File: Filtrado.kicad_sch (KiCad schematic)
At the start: 31 parts

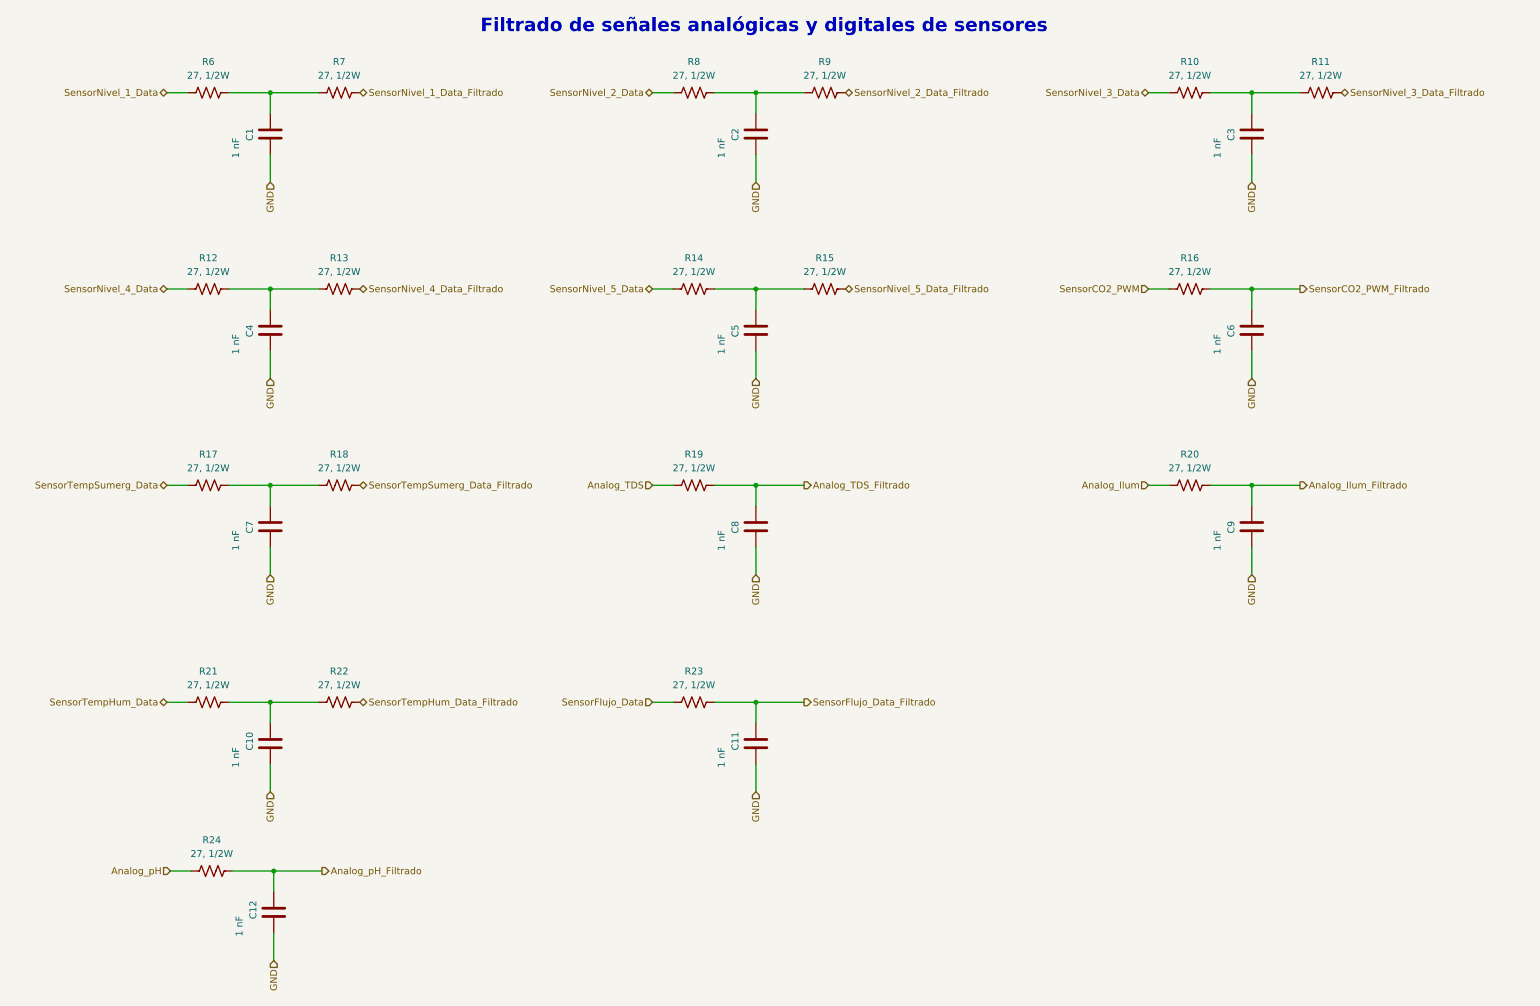
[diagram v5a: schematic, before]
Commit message: Se finalizó con el PCB del prototipo.
Dado que se buscó a toda costa que el PCB fuera de 1 capa, en varios puntos del circuito se tuvieron que agregar pin headers individuales para conectar a 3V3 y GND, junto con tiras de pin headers. Cada una de estas se conectara luego entre si mediante cables.

Tambien se generaron los archivos Gerber y BOM.
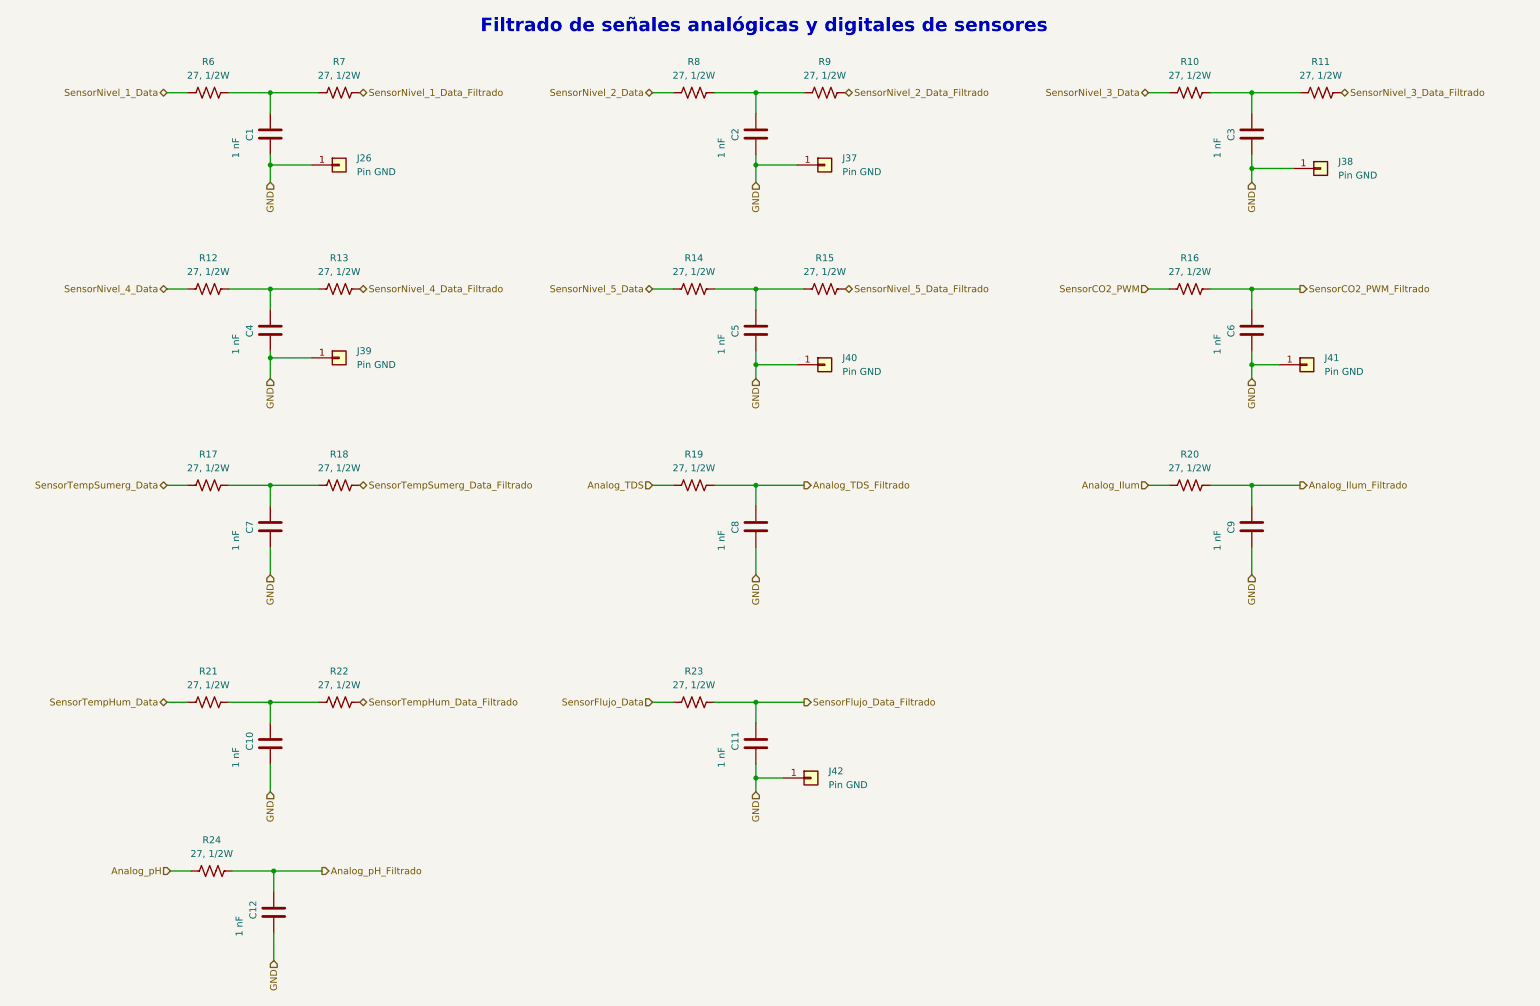
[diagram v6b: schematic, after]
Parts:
- added J26, J37, J38, J39, J40, J41, J42: Pin GND, Connector_PinHeader_2.54mm:PinHeader_1x01_P2.54mm_Vertical, symbol Connector_Generic:Conn_01x01
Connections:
- net GND: now also J26.1 (Pin_1), J37.1 (Pin_1), J38.1 (Pin_1), J39.1 (Pin_1), J40.1 (Pin_1), J41.1 (Pin_1), J42.1 (Pin_1)

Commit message: Se modificaron algunos componentes, según disponibilidad
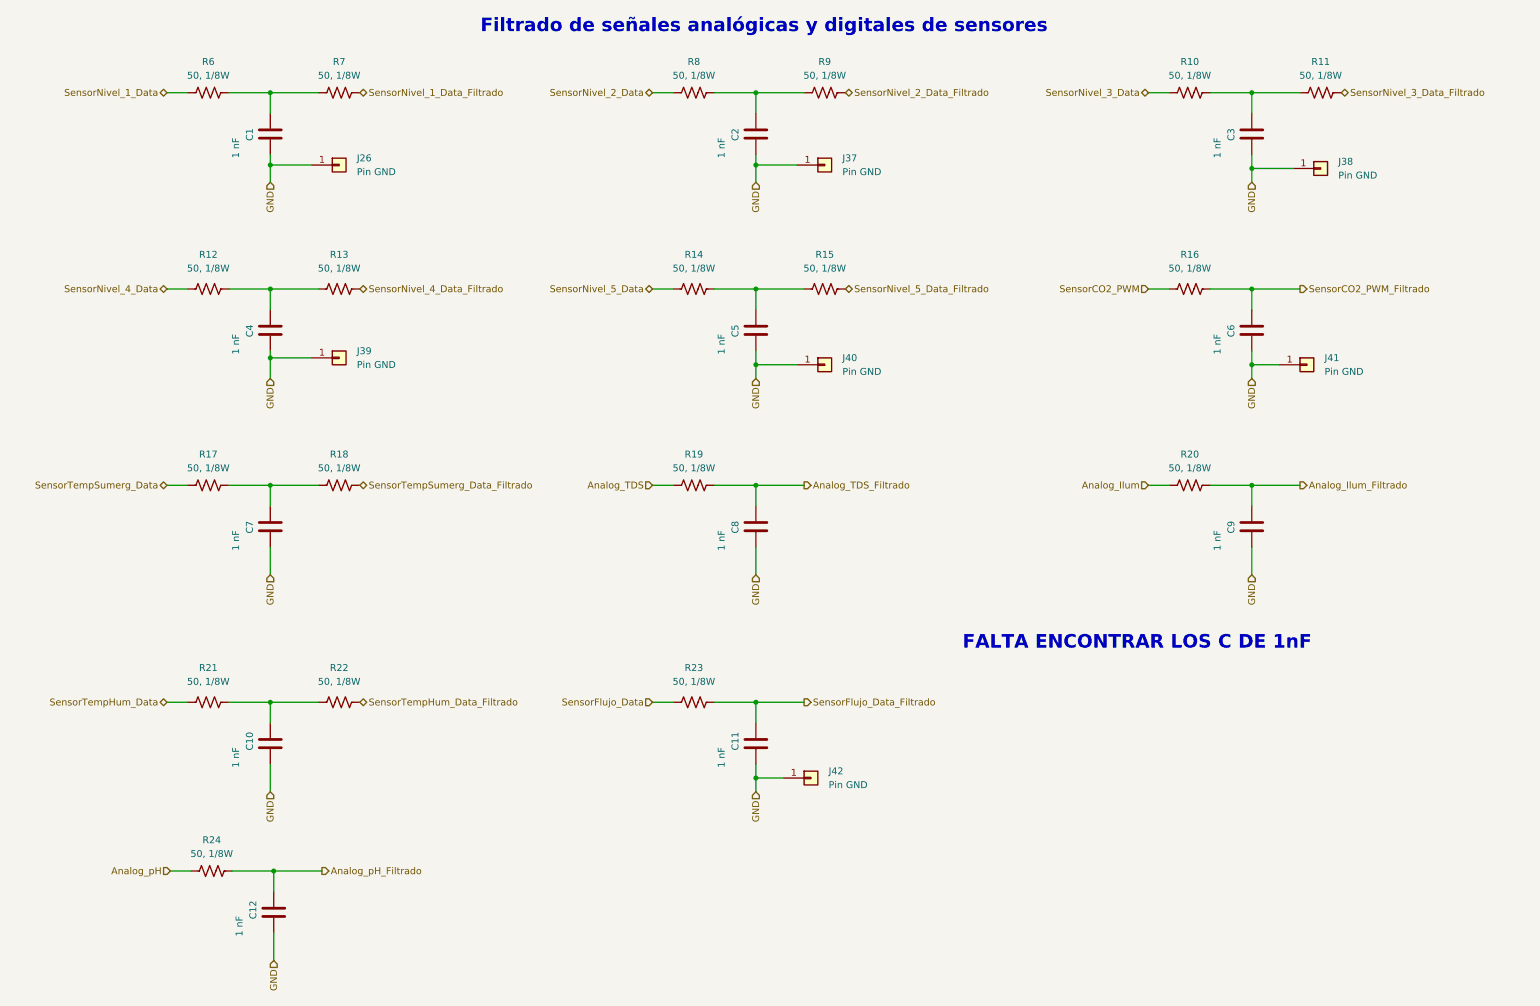
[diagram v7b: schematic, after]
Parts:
- R10, R11, R12, R13, R14, R15, R16, R17, R18, R19, R20, R21, R22, R23, R24, R6, R7, R8, R9: value 27, 1/2W -> 50, 1/8W
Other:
- note added: "FALTA ENCONTRAR LOS C DE 1nF"
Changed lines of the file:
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@@
     (stroke (width 0) (type default) (color 0 0 0 0))
+  )
+  (text "FALTA ENCONTRAR LOS C DE 1nF" (at 185.42 131.445 0)
+    (effects (font (size 2.5 2.5) (thickness 0.4) bold) (justify left bottom))
   )
   (text "Filtrado de señales analógicas y digitales de sensores"
@@
   (symbol (lib_id "Device:R_US") (at 160.02 64.77 90) (unit 1)
     (in_bom yes) (on_board yes) (fields_autoplaced)
-    (property "Reference" "R15" (id 0) (at 160.02 59.055 90))
-    (property "Value" "27, 1/2W" (id 1) (at 160.02 61.595 90))
+    (property "Reference" "R15" (id 0) (at 160.02 58.42 90))
+    (property "Value" "50, 1/8W" (id 1) (at 160.02 60.96 90))
     (property "Footprint" "Resistor_SMD:R_0805_2012Metric" (id 2) (at 160.274 63.754 90)
       (effects (font (size 1.27 1.27)) hide)
@@
     (in_bom yes) (on_board yes) (fields_autoplaced)
     (property "Reference" "R7" (id 0) (at 70.485 22.86 90))
-    (property "Value" "27, 1/2W" (id 1) (at 70.485 25.4 90))
+    (property "Value" "50, 1/8W" (id 1) (at 70.485 25.4 90))
     (property "Footprint" "Resistor_SMD:R_0805_2012Metric" (id 2) (at 70.739 27.559 90)
       (effects (font (size 1.27 1.27)) hide)
@@
   (symbol (lib_id "Device:R_US") (at 227.33 64.77 90) (unit 1)
     (in_bom yes) (on_board yes) (fields_autoplaced)
-    (property "Reference" "R16" (id 0) (at 227.33 59.055 90))
-    (property "Value" "27, 1/2W" (id 1) (at 227.33 61.595 90))
+    (property "Reference" "R16" (id 0) (at 227.33 58.42 90))
+    (property "Value" "50, 1/8W" (id 1) (at 227.33 60.96 90))
     (property "Footprint" "Resistor_SMD:R_0805_2012Metric" (id 2) (at 227.584 63.754 90)
       (effects (font (size 1.27 1.27)) hide)
@@
     (in_bom yes) (on_board yes) (fields_autoplaced)
     (property "Reference" "R24" (id 0) (at 46.99 166.37 90))
-    (property "Value" "27, 1/2W" (id 1) (at 46.99 168.91 90))
+    (property "Value" "50, 1/8W" (id 1) (at 46.99 168.91 90))
     (property "Footprint" "Resistor_SMD:R_0805_2012Metric" (id 2) (at 47.244 171.069 90)
       (effects (font (size 1.27 1.27)) hide)
@@
   (symbol (lib_id "Device:R_US") (at 135.89 64.77 90) (unit 1)
     (in_bom yes) (on_board yes) (fields_autoplaced)
-    (property "Reference" "R14" (id 0) (at 135.89 59.055 90))
-    (property "Value" "27, 1/2W" (id 1) (at 135.89 61.595 90))
+    (property "Reference" "R14" (id 0) (at 135.89 58.42 90))
+    (property "Value" "50, 1/8W" (id 1) (at 135.89 60.96 90))
     (property "Footprint" "Resistor_SMD:R_0805_2012Metric" (id 2) (at 136.144 63.754 90)
       (effects (font (size 1.27 1.27)) hide)
@@
     (in_bom yes) (on_board yes) (fields_autoplaced)
     (property "Reference" "R9" (id 0) (at 160.02 22.86 90))
-    (property "Value" "27, 1/2W" (id 1) (at 160.02 25.4 90))
+    (property "Value" "50, 1/8W" (id 1) (at 160.02 25.4 90))
     (property "Footprint" "Resistor_SMD:R_0805_2012Metric" (id 2) (at 160.274 27.559 90)
       (effects (font (size 1.27 1.27)) hide)
@@
   (symbol (lib_id "Device:R_US") (at 70.485 140.97 90) (unit 1)
     (in_bom yes) (on_board yes) (fields_autoplaced)
-    (property "Reference" "R22" (id 0) (at 70.485 135.255 90))
-    (property "Value" "27, 1/2W" (id 1) (at 70.485 137.795 90))
+    (property "Reference" "R22" (id 0) (at 70.485 134.62 90))
+    (property "Value" "50, 1/8W" (id 1) (at 70.485 137.16 90))
     (property "Footprint" "Resistor_SMD:R_0805_2012Metric" (id 2) (at 70.739 139.954 90)
       (effects (font (size 1.27 1.27)) hide)
@@
     (in_bom yes) (on_board yes) (fields_autoplaced)
     (property "Reference" "R19" (id 0) (at 135.89 95.25 90))
-    (property "Value" "27, 1/2W" (id 1) (at 135.89 97.79 90))
+    (property "Value" "50, 1/8W" (id 1) (at 135.89 97.79 90))
     (property "Footprint" "Resistor_SMD:R_0805_2012Metric" (id 2) (at 136.144 99.949 90)
       (effects (font (size 1.27 1.27)) hide)
@@
   (symbol (lib_id "Device:R_US") (at 46.355 140.97 90) (unit 1)
     (in_bom yes) (on_board yes) (fields_autoplaced)
-    (property "Reference" "R21" (id 0) (at 46.355 135.255 90))
-    (property "Value" "27, 1/2W" (id 1) (at 46.355 137.795 90))
+    (property "Reference" "R21" (id 0) (at 46.355 134.62 90))
+    (property "Value" "50, 1/8W" (id 1) (at 46.355 137.16 90))
     (property "Footprint" "Resistor_SMD:R_0805_2012Metric" (id 2) (at 46.609 139.954 90)
       (effects (font (size 1.27 1.27)) hide)
@@
   (symbol (lib_id "Device:R_US") (at 70.485 64.77 90) (unit 1)
     (in_bom yes) (on_board yes) (fields_autoplaced)
-    (property "Reference" "R13" (id 0) (at 70.485 59.055 90))
-    (property "Value" "27, 1/2W" (id 1) (at 70.485 61.595 90))
+    (property "Reference" "R13" (id 0) (at 70.485 58.42 90))
+    (property "Value" "50, 1/8W" (id 1) (at 70.485 60.96 90))
     (property "Footprint" "Resistor_SMD:R_0805_2012Metric" (id 2) (at 70.739 63.754 90)
       (effects (font (size 1.27 1.27)) hide)
@@
     (in_bom yes) (on_board yes) (fields_autoplaced)
     (property "Reference" "R20" (id 0) (at 227.33 95.25 90))
-    (property "Value" "27, 1/2W" (id 1) (at 227.33 97.79 90))
+    (property "Value" "50, 1/8W" (id 1) (at 227.33 97.79 90))
     (property "Footprint" "Resistor_SMD:R_0805_2012Metric" (id 2) (at 227.584 99.949 90)
       (effects (font (size 1.27 1.27)) hide)
@@
     (in_bom yes) (on_board yes) (fields_autoplaced)
     (property "Reference" "R8" (id 0) (at 135.89 22.86 90))
-    (property "Value" "27, 1/2W" (id 1) (at 135.89 25.4 90))
+    (property "Value" "50, 1/8W" (id 1) (at 135.89 25.4 90))
     (property "Footprint" "Resistor_SMD:R_0805_2012Metric" (id 2) (at 136.144 27.559 90)
       (effects (font (size 1.27 1.27)) hide)
@@
     (in_bom yes) (on_board yes) (fields_autoplaced)
     (property "Reference" "R11" (id 0) (at 251.46 22.86 90))
-    (property "Value" "27, 1/2W" (id 1) (at 251.46 25.4 90))
+    (property "Value" "50, 1/8W" (id 1) (at 251.46 25.4 90))
     (property "Footprint" "Resistor_SMD:R_0805_2012Metric" (id 2) (at 251.714 27.559 90)
       (effects (font (size 1.27 1.27)) hide)
@@
   (symbol (lib_id "Device:R_US") (at 135.89 140.97 90) (unit 1)
     (in_bom yes) (on_board yes) (fields_autoplaced)
-    (property "Reference" "R23" (id 0) (at 135.89 135.255 90))
-    (property "Value" "27, 1/2W" (id 1) (at 135.89 137.795 90))
+    (property "Reference" "R23" (id 0) (at 135.89 134.62 90))
+    (property "Value" "50, 1/8W" (id 1) (at 135.89 137.16 90))
     (property "Footprint" "Resistor_SMD:R_0805_2012Metric" (id 2) (at 136.144 139.954 90)
       (effects (font (size 1.27 1.27)) hide)
@@
     (in_bom yes) (on_board yes) (fields_autoplaced)
     (property "Reference" "R18" (id 0) (at 70.485 95.25 90))
-    (property "Value" "27, 1/2W" (id 1) (at 70.485 97.79 90))
+    (property "Value" "50, 1/8W" (id 1) (at 70.485 97.79 90))
     (property "Footprint" "Resistor_SMD:R_0805_2012Metric" (id 2) (at 70.739 99.949 90)
       (effects (font (size 1.27 1.27)) hide)
@@
     (in_bom yes) (on_board yes) (fields_autoplaced)
     (property "Reference" "R17" (id 0) (at 46.355 95.25 90))
-    (property "Value" "27, 1/2W" (id 1) (at 46.355 97.79 90))
+    (property "Value" "50, 1/8W" (id 1) (at 46.355 97.79 90))
     (property "Footprint" "Resistor_SMD:R_0805_2012Metric" (id 2) (at 46.609 99.949 90)
       (effects (font (size 1.27 1.27)) hide)
@@
     (in_bom yes) (on_board yes) (fields_autoplaced)
     (property "Reference" "R10" (id 0) (at 227.33 22.86 90))
-    (property "Value" "27, 1/2W" (id 1) (at 227.33 25.4 90))
+    (property "Value" "50, 1/8W" (id 1) (at 227.33 25.4 90))
     (property "Footprint" "Resistor_SMD:R_0805_2012Metric" (id 2) (at 227.584 27.559 90)
       (effects (font (size 1.27 1.27)) hide)
@@
   (symbol (lib_id "Device:R_US") (at 46.355 64.77 90) (unit 1)
     (in_bom yes) (on_board yes) (fields_autoplaced)
-    (property "Reference" "R12" (id 0) (at 46.355 59.055 90))
-    (property "Value" "27, 1/2W" (id 1) (at 46.355 61.595 90))
+    (property "Reference" "R12" (id 0) (at 46.355 58.42 90))
+    (property "Value" "50, 1/8W" (id 1) (at 46.355 60.96 90))
     (property "Footprint" "Resistor_SMD:R_0805_2012Metric" (id 2) (at 46.609 63.754 90)
       (effects (font (size 1.27 1.27)) hide)
@@
     (in_bom yes) (on_board yes) (fields_autoplaced)
     (property "Reference" "R6" (id 0) (at 46.355 22.86 90))
-    (property "Value" "27, 1/2W" (id 1) (at 46.355 25.4 90))
+    (property "Value" "50, 1/8W" (id 1) (at 46.355 25.4 90))
     (property "Footprint" "Resistor_SMD:R_0805_2012Metric" (id 2) (at 46.609 27.559 90)
       (effects (font (size 1.27 1.27)) hide)

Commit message: Actualización de backups.
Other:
- note removed: "FALTA ENCONTRAR LOS C DE 1nF"
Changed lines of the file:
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@@
     (stroke (width 0) (type default) (color 0 0 0 0))
-  )
-  (text "FALTA ENCONTRAR LOS C DE 1nF" (at 185.42 131.445 0)
-    (effects (font (size 2.5 2.5) (thickness 0.4) bold) (justify left bottom))
   )
   (text "Filtrado de señales analógicas y digitales de sensores"
